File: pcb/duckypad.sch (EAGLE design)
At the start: 135 parts, among them IC2 REG1117, SW1 SPST_TACT-EVQQ2, SW2 SPST_TACT-EVQQ2, SW21 EC12E_SW, SW22 EC12E_SW, SW3 324_SW324_SWITCH_FOOT_HOLE, U1 USBC_16P, U2 USBC_16P, U3 ESP32-S3FN8, Y1 16MHz_12pF

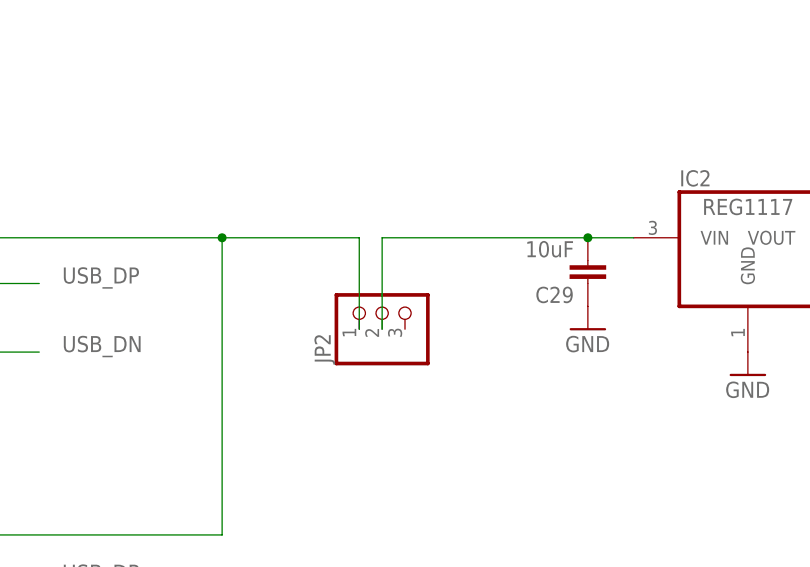
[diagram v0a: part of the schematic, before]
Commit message: switch cutout
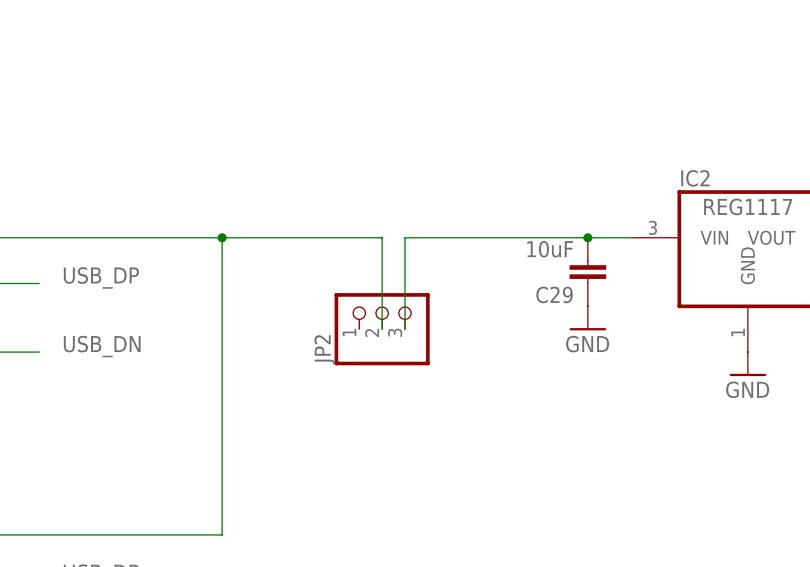
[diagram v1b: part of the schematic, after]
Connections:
- net N$1: now also JP2.2; no longer JP2.1
- net N$32: now also JP2.3; no longer JP2.2
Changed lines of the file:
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@@
 <wire x1="43.18" y1="-177.8" x2="78.74" y2="-177.8" width="0.1524" layer="91"/>
 <wire x1="78.74" y1="-177.8" x2="78.74" y2="-144.78" width="0.1524" layer="91"/>
-<pinref part="JP2" gate="A" pin="1"/>
-<wire x1="78.74" y1="-144.78" x2="93.98" y2="-144.78" width="0.1524" layer="91"/>
-<wire x1="93.98" y1="-144.78" x2="93.98" y2="-154.94" width="0.1524" layer="91"/>
+<wire x1="78.74" y1="-144.78" x2="96.52" y2="-144.78" width="0.1524" layer="91"/>
 <junction x="78.74" y="-144.78"/>
+<pinref part="JP2" gate="A" pin="2"/>
+<wire x1="96.52" y1="-144.78" x2="96.52" y2="-154.94" width="0.1524" layer="91"/>
 </segment>
 </net>
@@
 <pinref part="C29" gate="G$1" pin="2"/>
 <wire x1="119.38" y1="-144.78" x2="124.46" y2="-144.78" width="0.1524" layer="91"/>
-<wire x1="119.38" y1="-144.78" x2="96.52" y2="-144.78" width="0.1524" layer="91"/>
+<wire x1="119.38" y1="-144.78" x2="99.06" y2="-144.78" width="0.1524" layer="91"/>
 <junction x="119.38" y="-144.78"/>
-<pinref part="JP2" gate="A" pin="2"/>
-<wire x1="96.52" y1="-144.78" x2="96.52" y2="-154.94" width="0.1524" layer="91"/>
-</segment>
-</net>
+<pinref part="JP2" gate="A" pin="3"/>
+<wire x1="99.06" y1="-154.94" x2="99.06" y2="-144.78" width="0.1524" layer="91"/>
+</segment>
+</net>

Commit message: finishing touches
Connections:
- net N$1: now also JP2.1; no longer JP2.2
- net N$32: now also JP2.2; no longer JP2.3
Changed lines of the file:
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@@
 <wire x1="43.18" y1="-177.8" x2="78.74" y2="-177.8" width="0.1524" layer="91"/>
 <wire x1="78.74" y1="-177.8" x2="78.74" y2="-144.78" width="0.1524" layer="91"/>
-<wire x1="78.74" y1="-144.78" x2="96.52" y2="-144.78" width="0.1524" layer="91"/>
+<wire x1="78.74" y1="-144.78" x2="93.98" y2="-144.78" width="0.1524" layer="91"/>
 <junction x="78.74" y="-144.78"/>
-<pinref part="JP2" gate="A" pin="2"/>
-<wire x1="96.52" y1="-144.78" x2="96.52" y2="-154.94" width="0.1524" layer="91"/>
+<pinref part="JP2" gate="A" pin="1"/>
+<wire x1="93.98" y1="-144.78" x2="93.98" y2="-154.94" width="0.1524" layer="91"/>
 </segment>
 </net>
@@
 <pinref part="C29" gate="G$1" pin="2"/>
 <wire x1="119.38" y1="-144.78" x2="124.46" y2="-144.78" width="0.1524" layer="91"/>
-<wire x1="119.38" y1="-144.78" x2="99.06" y2="-144.78" width="0.1524" layer="91"/>
+<wire x1="119.38" y1="-144.78" x2="96.52" y2="-144.78" width="0.1524" layer="91"/>
 <junction x="119.38" y="-144.78"/>
-<pinref part="JP2" gate="A" pin="3"/>
-<wire x1="99.06" y1="-154.94" x2="99.06" y2="-144.78" width="0.1524" layer="91"/>
-</segment>
-</net>
+<pinref part="JP2" gate="A" pin="2"/>
+<wire x1="96.52" y1="-144.78" x2="96.52" y2="-154.94" width="0.1524" layer="91"/>
+</segment>
+</net>

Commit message: ready for prod
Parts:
- removed JP3: (no value), adafruit_changed:PINHD-1X1CB
- added JP5: (no value), pinhead:PINHD-2X3
- added R16: 10K, joyAnalog:RESISTOR0805-RES
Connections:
- removed net N$44: U$2.DC, U3.GPIO11
- removed net N$45: R12.1, U$2.CS, U3.GPIO12
- new net DC: JP5.3, U$2.DC, U3.GPIO11
- new net OLED_CS: JP5.1, R12.1, U$2.CS, U3.GPIO12
- net +3V3: now also R16.2
- net GND: now also JP5.6
- net MOSI: now also JP5.5
- net N$41: now also R16.1
- net RESET: now also JP5.2; no longer JP3.1
- net SCLK: now also JP5.4
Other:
- moved on the sheet: SW21

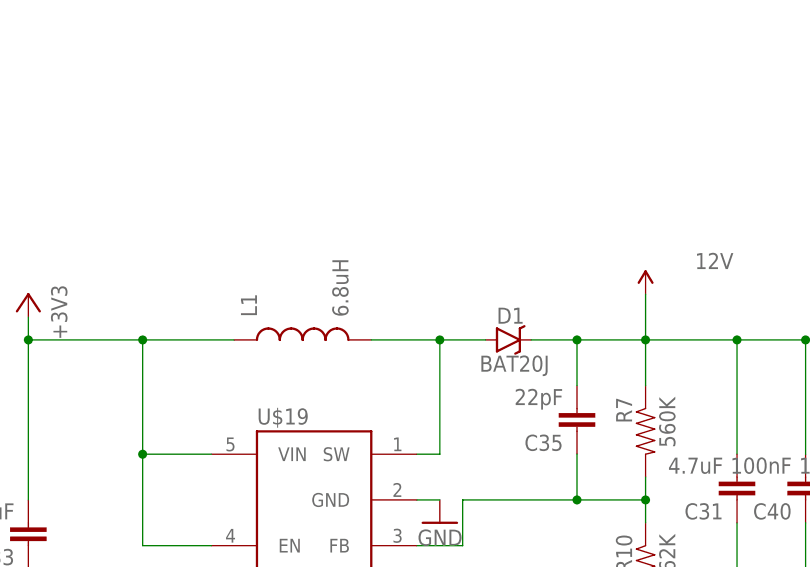
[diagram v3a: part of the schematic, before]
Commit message: updated inductor footprint
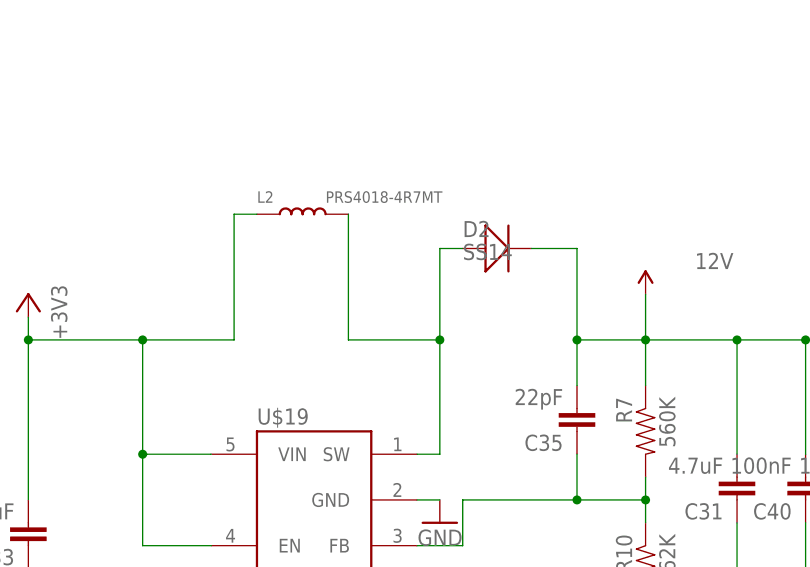
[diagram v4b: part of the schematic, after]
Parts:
- removed D1: BAT20J, SparkFun-DiscreteSemi:DIODE-SCHOTTKY-BAT20J
- removed L1: 6.8uH, basicBoard:INDUCTOR0805
- added D2: SS14, Discrete_NOA:D214AA
- added L2: PRS4018-4R7MT, Discrete:L-4030
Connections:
- net +3V3: now also L2.1; no longer L1.1
- net 12V: now also D2.-; no longer D1.C
- net N$36: now also D2.+, L2.2; no longer D1.A, L1.2
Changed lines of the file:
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@@
 <part name="GND44" library="supply1" deviceset="GND" device=""/>
 <part name="C33" library="clock" deviceset="CAP" device="0805" value="4.7uF"/>
-<part name="L1" library="basicBoard" deviceset="INDUCTOR" device="0805" value="6.8uH"/>
-<part name="D1" library="SparkFun-DiscreteSemi" deviceset="DIODE-SCHOTTKY" device="-BAT20J" value="BAT20J"/>
 <part name="SUPPLY2" library="SparkFun-PowerSymbols" deviceset="12V" device=""/>
 <part name="C35" library="clock" deviceset="CAP" device="0805" value="22pF"/>
@@
 <part name="R16" library="joyAnalog" deviceset="RESISTOR" device="0805-RES" value="10K"/>
 <part name="+3V35" library="supply1" library_urn="urn:adsk.eagle:library:371" deviceset="+3V3" device=""/>
+<part name="L2" library="Discrete" deviceset="L*" device="-4030" value="PRS4018-4R7MT"/>
+<part name="D2" library="Discrete_NOA" library_urn="urn:adsk.eagle:library:2000212" deviceset="D*" device="214AA" package3d_urn="urn:adsk.eagle:package:2068475/4" value="SS14"/>
 </parts>
 <sheets>
@@
 <attribute name="VALUE" x="158.496" y="-284.861" size="1.778" layer="96" rot="R180"/>
 </instance>
-<instance part="L1" gate="G$1" x="190.5" y="-266.7" smashed="yes" rot="R90">
-<attribute name="NAME" x="185.42" y="-264.16" size="1.778" layer="95" rot="R90"/>
-<attribute name="VALUE" x="195.58" y="-264.16" size="1.778" layer="96" rot="R90"/>
-</instance>
-<instance part="D1" gate="G$1" x="213.36" y="-266.7" smashed="yes">
-<attribute name="NAME" x="215.138" y="-263.1186" size="1.778" layer="95" rot="R180"/>
-<attribute name="VALUE" x="217.932" y="-268.4526" size="1.778" layer="96" rot="R180"/>
-</instance>
 <instance part="SUPPLY2" gate="G$1" x="228.6" y="-261.62" smashed="yes">
 <attribute name="VALUE" x="236.22" y="-258.826" size="1.778" layer="96" align="bottom-center"/>
@@
 <instance part="+3V35" gate="G$1" x="457.2" y="-45.72" smashed="yes" rot="MR0">
 <attribute name="VALUE" x="459.74" y="-50.8" size="1.778" layer="96" rot="MR90"/>
+</instance>
+<instance part="L2" gate="L" x="190.5" y="-252.73" smashed="yes">
+<attribute name="NAME" x="185.42" y="-251.46" size="1.27" layer="95"/>
+<attribute name="VALUE" x="193.04" y="-251.46" size="1.27" layer="96"/>
+</instance>
+<instance part="D2" gate="D" x="212.09" y="-256.54" smashed="yes">
+<attribute name="NAME" x="208.28" y="-255.27" size="1.778" layer="95" ratio="10"/>
+<attribute name="VALUE" x="208.28" y="-257.81" size="1.778" layer="96" ratio="10"/>
 </instance>
 </instances>
@@
 <pinref part="C33" gate="G$1" pin="2"/>
 <wire x1="160.02" y1="-264.16" x2="160.02" y2="-266.7" width="0.1524" layer="91"/>
-<pinref part="L1" gate="G$1" pin="1"/>
 <wire x1="160.02" y1="-266.7" x2="160.02" y2="-284.48" width="0.1524" layer="91"/>
 <wire x1="160.02" y1="-266.7" x2="172.72" y2="-266.7" width="0.1524" layer="91"/>
@@
 <wire x1="172.72" y1="-289.56" x2="172.72" y2="-279.4" width="0.1524" layer="91"/>
 <junction x="172.72" y="-279.4"/>
+<pinref part="L2" gate="L" pin="1"/>
+<wire x1="185.42" y1="-252.73" x2="182.88" y2="-252.73" width="0.1524" layer="91"/>
+<wire x1="182.88" y1="-252.73" x2="182.88" y2="-266.7" width="0.1524" layer="91"/>
 </segment>
 <segment>
@@
 <pinref part="R7" gate="G$1" pin="1"/>
 <wire x1="228.6" y1="-271.78" x2="228.6" y2="-266.7" width="0.1524" layer="91"/>
-<pinref part="D1" gate="G$1" pin="C"/>
 <wire x1="228.6" y1="-266.7" x2="228.6" y2="-261.62" width="0.1524" layer="91"/>
-<wire x1="215.9" y1="-266.7" x2="220.98" y2="-266.7" width="0.1524" layer="91"/>
 <junction x="228.6" y="-266.7"/>
 <pinref part="C35" gate="G$1" pin="2"/>
@@
 <wire x1="246.38" y1="-279.4" x2="246.38" y2="-266.7" width="0.1524" layer="91"/>
 <junction x="246.38" y="-266.7"/>
+<pinref part="D2" gate="D" pin="-"/>
+<wire x1="215.9" y1="-256.54" x2="220.98" y2="-256.54" width="0.1524" layer="91"/>
+<wire x1="220.98" y1="-256.54" x2="220.98" y2="-266.7" width="0.1524" layer="91"/>
 </segment>
 <segment>
@@
 <net name="N$36" class="0">
 <segment>
-<pinref part="L1" gate="G$1" pin="2"/>
-<wire x1="198.12" y1="-266.7" x2="205.74" y2="-266.7" width="0.1524" layer="91"/>
-<pinref part="D1" gate="G$1" pin="A"/>
+<wire x1="195.58" y1="-266.7" x2="205.74" y2="-266.7" width="0.1524" layer="91"/>
 <pinref part="U$19" gate="G$1" pin="SW"/>
-<wire x1="205.74" y1="-266.7" x2="210.82" y2="-266.7" width="0.1524" layer="91"/>
 <wire x1="203.2" y1="-279.4" x2="205.74" y2="-279.4" width="0.1524" layer="91"/>
 <wire x1="205.74" y1="-279.4" x2="205.74" y2="-266.7" width="0.1524" layer="91"/>
 <junction x="205.74" y="-266.7"/>
-</segment>
-</net>
+<pinref part="L2" gate="L" pin="2"/>
+<wire x1="195.58" y1="-252.73" x2="195.58" y2="-266.7" width="0.1524" layer="91"/>
+<pinref part="D2" gate="D" pin="+"/>
+<wire x1="208.28" y1="-256.54" x2="205.74" y2="-256.54" width="0.1524" layer="91"/>
+<wire x1="205.74" y1="-256.54" x2="205.74" y2="-266.7" width="0.1524" layer="91"/>
+</segment>
+</net>

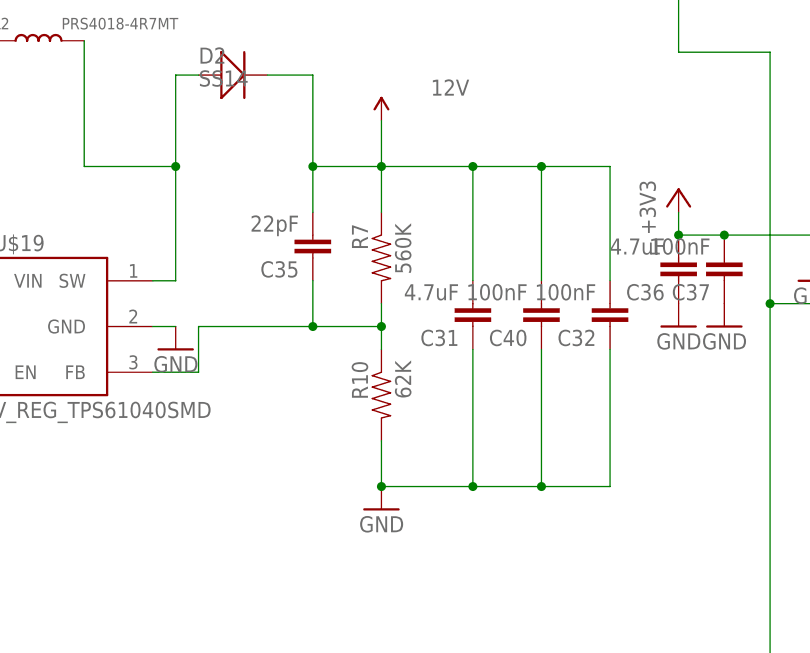
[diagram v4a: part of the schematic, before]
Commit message: updated inductor footprint
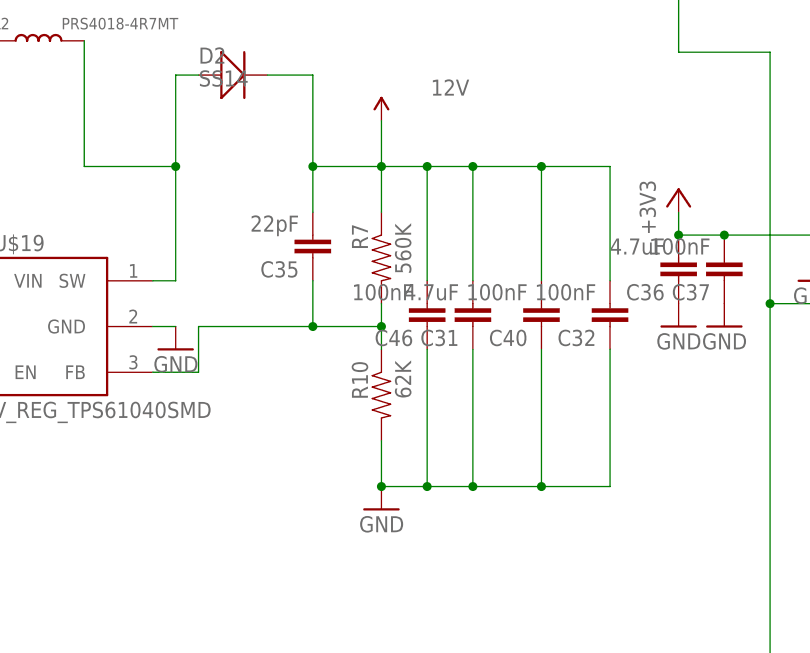
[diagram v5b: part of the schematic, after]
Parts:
- added C46: 100nF, clock:CAP0805
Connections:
- net 12V: now also C46.2
- net GND: now also C46.1
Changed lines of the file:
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@@
 <part name="L2" library="Discrete" deviceset="L*" device="-4030" value="PRS4018-4R7MT"/>
 <part name="D2" library="Discrete_NOA" library_urn="urn:adsk.eagle:library:2000212" deviceset="D*" device="214AA" package3d_urn="urn:adsk.eagle:package:2068475/4" value="SS14"/>
+<part name="C46" library="clock" deviceset="CAP" device="0805" value="100nF"/>
 </parts>
 <sheets>
@@
 <attribute name="NAME" x="208.28" y="-255.27" size="1.778" layer="95" ratio="10"/>
 <attribute name="VALUE" x="208.28" y="-257.81" size="1.778" layer="96" ratio="10"/>
+</instance>
+<instance part="C46" gate="G$1" x="233.68" y="-281.94" smashed="yes" rot="R180">
+<attribute name="NAME" x="232.156" y="-284.861" size="1.778" layer="95" rot="R180"/>
+<attribute name="VALUE" x="232.156" y="-279.781" size="1.778" layer="96" rot="R180"/>
 </instance>
 </instances>
@@
 <wire x1="228.6" y1="-297.18" x2="228.6" y2="-302.26" width="0.1524" layer="91"/>
 <pinref part="C31" gate="G$1" pin="1"/>
-<wire x1="228.6" y1="-302.26" x2="238.76" y2="-302.26" width="0.1524" layer="91"/>
+<wire x1="228.6" y1="-302.26" x2="233.68" y2="-302.26" width="0.1524" layer="91"/>
+<wire x1="233.68" y1="-302.26" x2="238.76" y2="-302.26" width="0.1524" layer="91"/>
 <wire x1="238.76" y1="-302.26" x2="238.76" y2="-287.02" width="0.1524" layer="91"/>
 <junction x="228.6" y="-302.26"/>
@@
 <wire x1="246.38" y1="-287.02" x2="246.38" y2="-302.26" width="0.1524" layer="91"/>
 <junction x="246.38" y="-302.26"/>
+<pinref part="C46" gate="G$1" pin="1"/>
+<wire x1="233.68" y1="-287.02" x2="233.68" y2="-302.26" width="0.1524" layer="91"/>
+<junction x="233.68" y="-302.26"/>
 </segment>
 <segment>
@@
 <junction x="220.98" y="-266.7"/>
 <pinref part="C31" gate="G$1" pin="2"/>
-<wire x1="228.6" y1="-266.7" x2="238.76" y2="-266.7" width="0.1524" layer="91"/>
+<wire x1="228.6" y1="-266.7" x2="233.68" y2="-266.7" width="0.1524" layer="91"/>
+<wire x1="233.68" y1="-266.7" x2="238.76" y2="-266.7" width="0.1524" layer="91"/>
 <wire x1="238.76" y1="-266.7" x2="238.76" y2="-279.4" width="0.1524" layer="91"/>
 <pinref part="C32" gate="G$1" pin="2"/>
@@
 <wire x1="215.9" y1="-256.54" x2="220.98" y2="-256.54" width="0.1524" layer="91"/>
 <wire x1="220.98" y1="-256.54" x2="220.98" y2="-266.7" width="0.1524" layer="91"/>
-</segment>
-<segment>
+<pinref part="C46" gate="G$1" pin="2"/>
+<wire x1="233.68" y1="-266.7" x2="233.68" y2="-279.4" width="0.1524" layer="91"/>
+<junction x="233.68" y="-266.7"/>
+</segment>
+<segment>
